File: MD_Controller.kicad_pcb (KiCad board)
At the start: 2 copper layers, 99.1 x 78.7 mm, 72 parts, among them M1 minibed

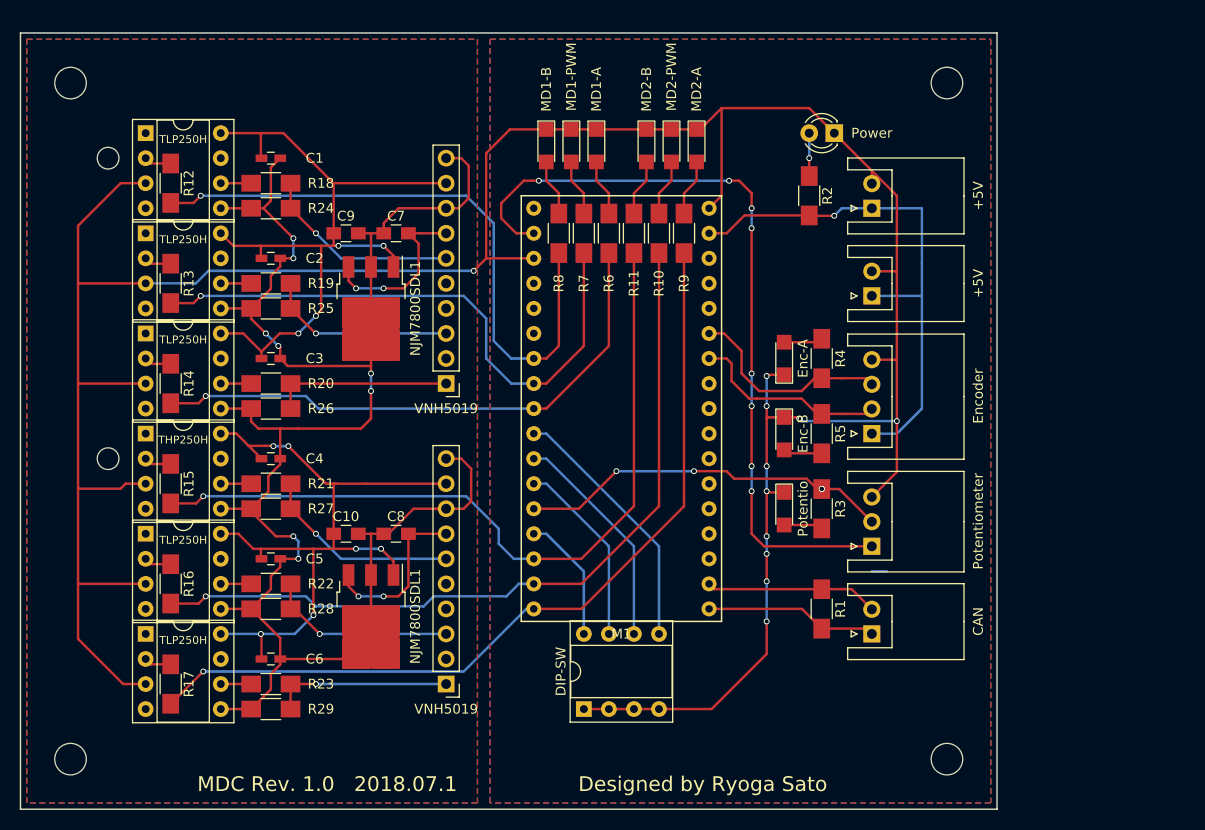
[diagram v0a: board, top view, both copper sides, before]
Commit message: 2.0.1
入力ポートの増設
電流センサの外部出力ポートの増設
UARTポートの増設
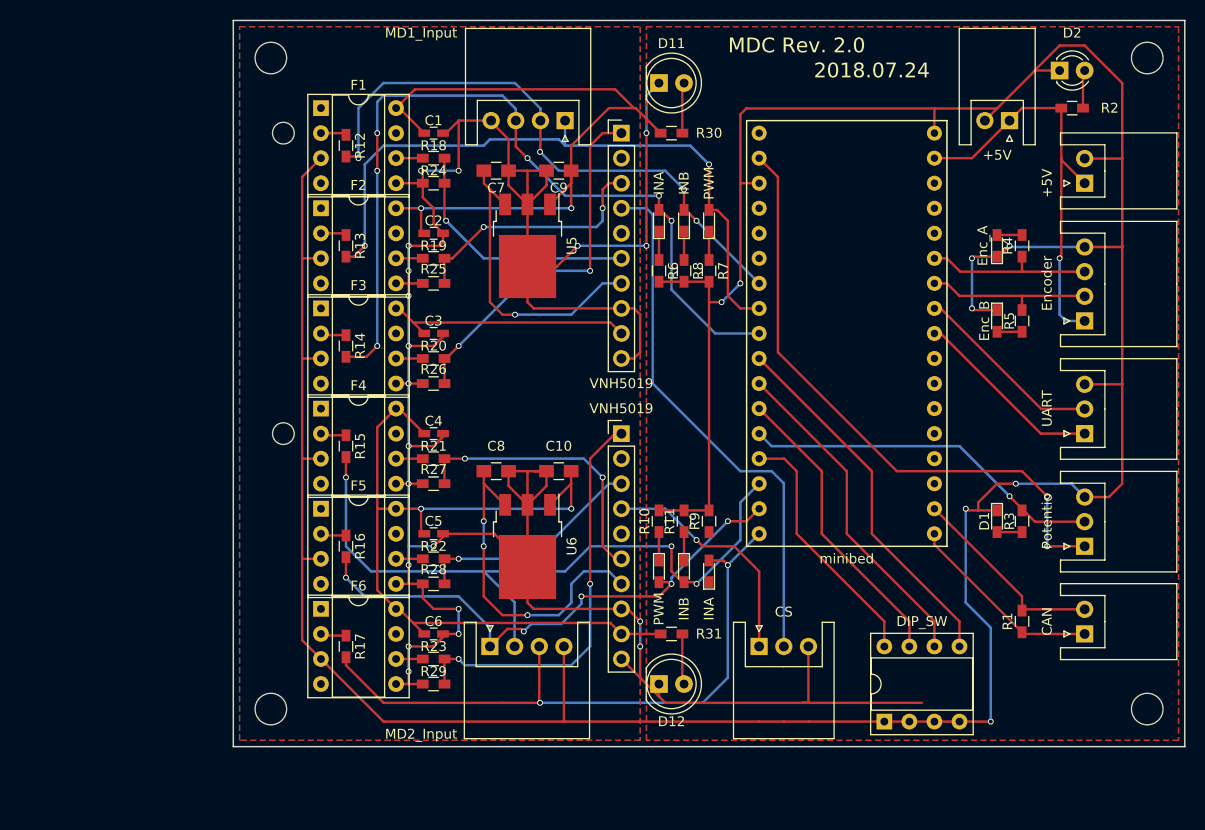
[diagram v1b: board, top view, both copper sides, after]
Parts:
- removed the +5V at (177.8, 76.2)
- removed the +5V at (177.8, 85.1)
- removed DIP-SW: dipSW, Housings_DIP:DIP-8_W7.62mm_Socket
- removed Enc-A, Enc-B, MD1-A, MD1-B, MD1-PWM, MD2-A, MD2-B, MD2-PWM: LED, LEDs:LED_1206
- removed M1: minibed, MyLibs:minibed
- removed NJM7800SDL1 (x2): NJM7800SDL1, TO_SOT_Packages_SMD:TO-252-3_TabPin2
- removed the Potentio at (168.9, 106.7)
- removed Potentiometer: potentio__connector, Connectors_JST:JST_XH_S03B-XH-A_03x2.50mm_Angled
- removed Power: LED, LEDs:LED_D3.0mm_FlatTop
- removed THP250H, TLP250H (x5): TLP250H, Housings_DIP:DIP-8_W7.62mm_Socket
- removed the VNH5019 at (134.6, 94.0)
- removed the VNH5019 at (134.6, 124.5)
- added +5V: XH_2, Connectors_JST:JST_XH_S02B-XH-A_02x2.50mm_Angled, F.Cu at (199.4, 73.7)
- added +5V: XH_2, Connectors_JST:JST_XH_S02B-XH-A_02x2.50mm_Angled, F.Cu at (191.8, 67.3)
- added CS: XH_3, Connectors_JST:JST_XH_S03B-XH-A_03x2.50mm_Angled, F.Cu at (166.4, 120.7)
- added D1: LED, LEDs:LED_0603_HandSoldering, F.Cu at (190.5, 108.0)
- added D11: LED, LEDs:LED_D5.0mm_FlatTop, F.Cu at (156.2, 63.5)
- added D12: LED, LEDs:LED_D5.0mm_FlatTop, F.Cu at (156.2, 124.5)
- added D2: LED, LEDs:LED_D3.0mm_FlatTop, F.Cu at (196.8, 62.2)
- added DIP_SW: dipSW, Housings_DIP:DIP-8_W7.62mm_Socket, F.Cu at (179.1, 128.3)
- added Enc_A: LED, LEDs:LED_0603_HandSoldering, F.Cu at (190.5, 80.0)
- added Enc_B: LED, LEDs:LED_0603_HandSoldering, F.Cu at (190.5, 87.6)
- added F1: TLP250H, Housings_DIP:DIP-8_W7.62mm_Socket, F.Cu at (121.9, 66.0)
- added F2: TLP250H, Housings_DIP:DIP-8_W7.62mm_Socket, F.Cu at (121.9, 76.2)
- added F3: TLP250H, Housings_DIP:DIP-8_W7.62mm_Socket, F.Cu at (121.9, 86.4)
- added F4: TLP250H, Housings_DIP:DIP-8_W7.62mm_Socket, F.Cu at (121.9, 96.5)
- added F5: TLP250H, Housings_DIP:DIP-8_W7.62mm_Socket, F.Cu at (121.9, 106.7)
- added F6: TLP250H, Housings_DIP:DIP-8_W7.62mm_Socket, F.Cu at (121.9, 116.8)
- added INA: LED, LEDs:LED_0603_HandSoldering, F.Cu at (156.2, 77.5)
- added INA: LED, LEDs:LED_0603_HandSoldering, F.Cu at (161.3, 113.0)
- added INB: LED, LEDs:LED_0603_HandSoldering, F.Cu at (158.8, 77.5)
- added INB: LED, LEDs:LED_0603_HandSoldering, F.Cu at (158.8, 113.0)
- added MD1_Input: XH_4, Connectors_JST:JST_XH_S04B-XH-A_04x2.50mm_Angled, F.Cu at (146.7, 67.3)
- added MD2_Input: XH_4, Connectors_JST:JST_XH_S04B-XH-A_04x2.50mm_Angled, F.Cu at (139.1, 120.7)
- added PWM: LED, LEDs:LED_0603_HandSoldering, F.Cu at (161.3, 77.5)
- added PWM: LED, LEDs:LED_0603_HandSoldering, F.Cu at (156.2, 113.0)
- added Potentio: potentio__connector, Connectors_JST:JST_XH_S03B-XH-A_03x2.50mm_Angled, F.Cu at (199.4, 110.5)
- added R30: R, Resistors_SMD:R_0603_HandSoldering, F.Cu at (157.5, 68.6)
- added R31: R, Resistors_SMD:R_0603_HandSoldering, F.Cu at (157.5, 119.4)
- added U5: NJM7800SDL1, TO_SOT_Packages_SMD:TO-252-3_TabPin2, F.Cu at (142.9, 80.0)
- added U6: NJM7800SDL1, TO_SOT_Packages_SMD:TO-252-3_TabPin2, F.Cu at (142.9, 110.5)
- added UART: XH_3, Connectors_JST:JST_XH_S03B-XH-A_03x2.50mm_Angled, F.Cu at (199.4, 99.1)
- added VNH5019: VNH5019, Pin_Headers:Pin_Header_Straight_1x10_Pitch2.54mm, F.Cu at (152.4, 68.6)
- added VNH5019: VNH5019, Pin_Headers:Pin_Header_Straight_1x10_Pitch2.54mm, F.Cu at (152.4, 99.1)
- added minibed: minibed, MyLibs:minibed, F.Cu at (175.3, 88.9)
- R1, R10, R11, R12, R13, R14, R15, R16, R17, R18, R19, R2, R20, R21, R22, R23, R24, R25, R26, R27, R28, R29, R3, R4, R5, R6, R7, R8, R9: footprint Resistors_SMD:R_1206_HandSoldering -> Resistors_SMD:R_0603_HandSoldering
- moved R11 29.6 mm to (158.8, 108.0)
- moved R9 29.3 mm to (161.3, 108.0)
- moved R10 29.2 mm to (156.2, 108.0)
- moved R2 28.1 mm to (198.1, 66.0), turned to 180 degrees
- moved Encoder 24.4 mm to (199.4, 87.6)
- moved R5 23.3 mm to (193.0, 87.6)
- moved R4 23.3 mm to (193.0, 80.0)
- moved C10 22.5 mm to (146.1, 102.9), turned to 180 degrees
- moved C9 22.5 mm to (146.1, 72.4), turned to 180 degrees
- moved CAN 21.6 mm to (199.4, 119.4)
- moved ? 20.9 mm to (205.7, 127.0)
- moved ? 20.9 mm to (116.8, 127.0)
- moved ? 20.5 mm to (205.7, 61.0)
- moved ? 20.5 mm to (116.8, 61.0)
- moved R1 20.4 mm to (193.0, 118.1)
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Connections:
- R10 pad 1: p8 -> Net-(D9-Pad1)
- R10 pad 2: Net-(D9-Pad2) -> GNDA
- R11 pad 1: p7 -> Net-(D10-Pad1)
- R11 pad 2: Net-(D10-Pad2) -> GNDA
- R6 pad 1: p0 -> Net-(D5-Pad1)
- R6 pad 2: Net-(D5-Pad2) -> GNDA
- R7 pad 1: p25 -> Net-(D6-Pad1)
- R7 pad 2: Net-(D6-Pad2) -> GNDA
- R8 pad 1: p24 -> Net-(D7-Pad1)
- R8 pad 2: Net-(D7-Pad2) -> GNDA
- R9 pad 1: p9 -> Net-(D8-Pad1)
- R9 pad 2: Net-(D8-Pad2) -> GNDA
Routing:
- net GND: track 185.2 -> 279.7 mm, vias 8 -> 20
- net GNDA: track 300.9 -> 360.0 mm, vias 11 -> 8
- net CS_1: track 0.00 -> 54.6 mm
- net p0: track 57.3 -> 84.6 mm, vias 1 -> 6
- net CS_2: track 0.00 -> 24.2 mm, vias 0 -> 1
- net p8: track 80.1 -> 56.1 mm, vias 1 -> 5
- net VOUT1: track 74.7 -> 98.2 mm, vias 4 -> 2
- net INA2: track 18.3 -> 41.6 mm, vias 1 -> 2
- net p9: track 86.1 -> 66.0 mm, vias 1 -> 2
- net p17: track 0.00 -> 19.5 mm
- net p15: track 0.00 -> 19.4 mm
- net INA1: track 18.3 -> 37.4 mm, vias 0 -> 2
- net +3V3: track 79.9 -> 62.7 mm, vias 8 -> 2
- net Net-(C8-Pad2): track 18.7 -> 34.0 mm, vias 2 -> 3
- net Net-(C7-Pad2): track 17.8 -> 30.9 mm, vias 2 -> 1
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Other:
- board size 99.1 x 78.7 mm -> 96.5 x 73.7 mm
- board text added: "2018.07.24"
- board text added: "MDC Rev. 2.0"
- board text removed: "Designed by Ryoga Sato"
- board text removed: "MDC Rev. 1.0 2018.07.1"
